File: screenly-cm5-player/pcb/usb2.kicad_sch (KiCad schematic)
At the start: 8 parts, among them J7 10.0 QHHTZB6.3, U7 AP22652W6-7

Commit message: Finished USB
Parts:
- removed R28: 100K, Screenly:R_0402, symbol Screenly:Resistor 100K 1% 0402 (0402WGF1003TCE)
- added R28: 31.6K, Screenly:R_0402, symbol Screenly:Resistor 31.6K 1% 0402 (0402WGF3162TCE)
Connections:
- net GND: now also J7.4 (GND), J7.SH, R28.2
- net at U7.5 (ILIM): now also R28.1
- net +5V renamed +5V_USB

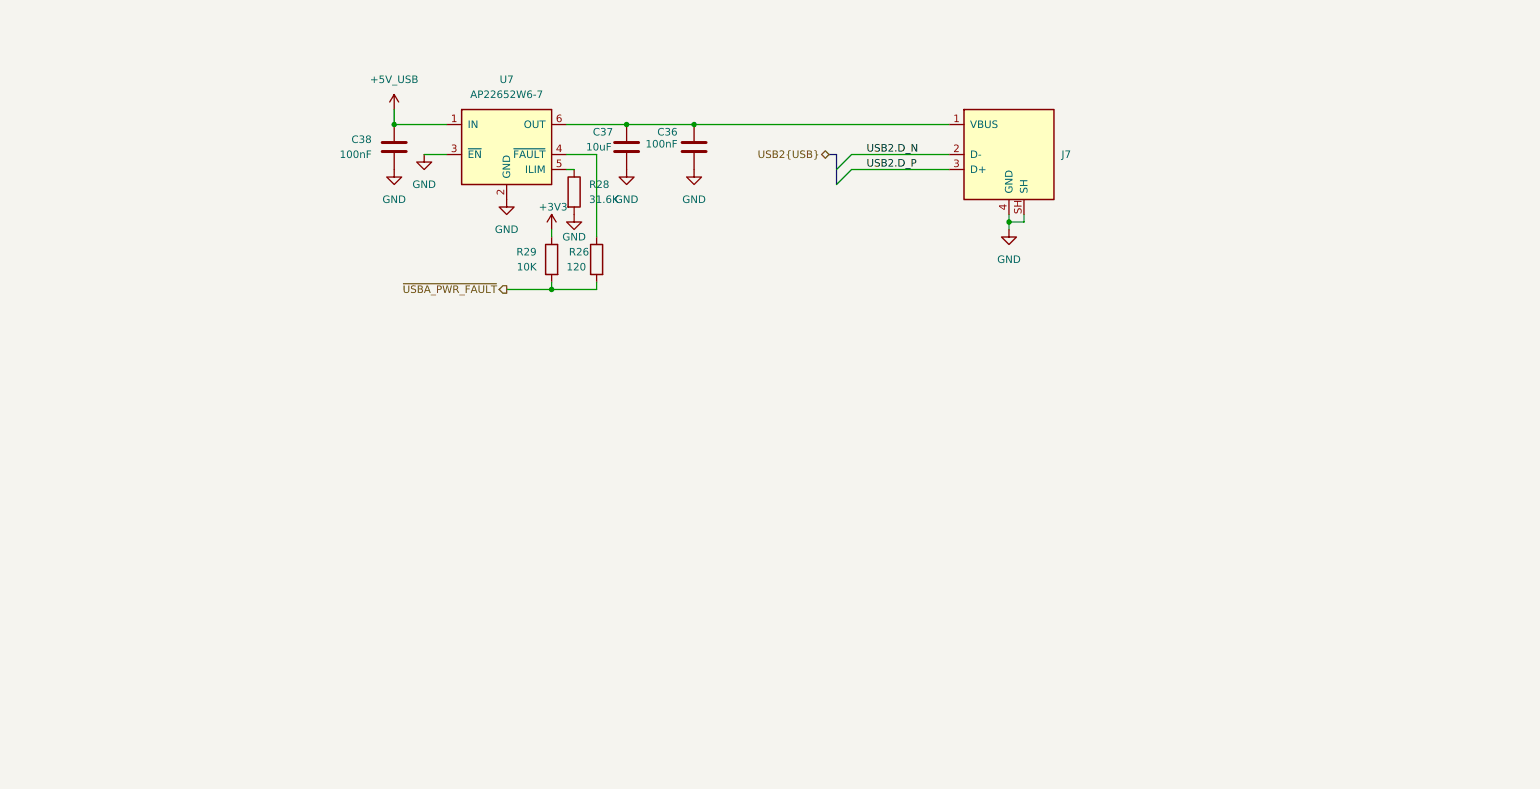
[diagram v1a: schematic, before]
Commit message: Revised USB design 1xUSB-C 2.0, 2xUSB-A 3.0
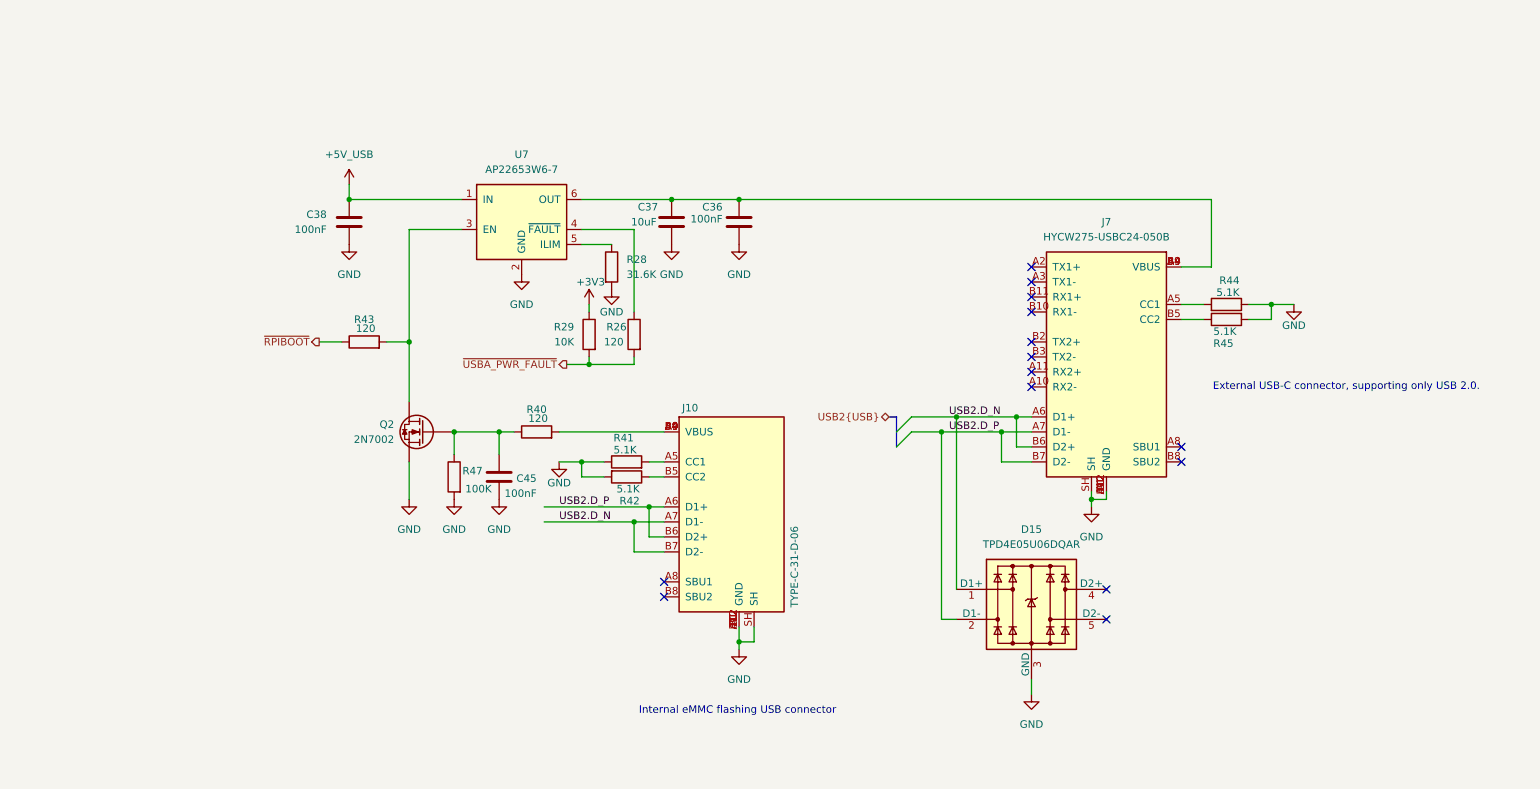
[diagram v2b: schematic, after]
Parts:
- removed J7: 10.0 QHHTZB6.3, Screenly:USB_A_SHOUHAN_QHHTZB6.3_Horizontal, symbol Screenly:USB-A Receptacle USB 2.0 SMD (10.0 QHHTZB6.3)
- removed U7: AP22652W6-7, Screenly:SOT-23-6, symbol Screenly:Power Switch 3-5.5V 2.1A SOT-23-6 (AP22652W6-7)
- added C45: 100nF, Screenly:C_0402, symbol Screenly:Capacitor 100nF 50V X7R 0402 (CL05B104KB54PNC)
- added D15: TPD4E05U06DQAR, Screenly:TI_USON-10_2.5x1.0mm_P0.5mm, symbol Screenly:ESD Diode 4ch 5.5V USON-10 (TPD4E05U06DQAR)
- added J10: TYPE-C-31-D-06, Screenly:USB_C_Receptacle_HRO_TYPE-C-31-D-06_Vertical, symbol Screenly:USB-C Receptacle 16P USB 2.0 Vertical SMD (TYPE-C-31-D-06)
- added J7: HYCW275-USBC24-050B, Screenly:USB_C_Receptacle_HOAUC_HYCW275-USBC24-050B, symbol Screenly:USB-C Receptacle 24P USB 3.1 SMD (HYCW275-USBC24-050B)
- added Q2: 2N7002, Screenly:SOT-23, symbol Screenly:N-MOSFET 60V 115mA 7.5Ohm SOT-23 (2N7002)
- added R40, R43: 120, Screenly:R_0402, symbol Screenly:Resistor 120R 5% 0402 (0402WGJ0121TCE)
- added R41, R42, R44, R45: 5.1K, Screenly:R_0402, symbol Screenly:Resistor 5.1K 1% 0402 (0402WGF5101TCE)
- added R47: 100K, Screenly:R_0402, symbol Screenly:Resistor 100K 1% 0402 (0402WGF1003TCE)
- added U7: AP22653W6-7, Screenly:SOT-23-6, symbol Screenly:Power Switch 3-5.5V 2.1A SOT-23-6 (AP22653W6-7)
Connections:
- net +5V_USB: now also U7.1 (IN)
- net GND: now also C45.2, D15.3 (GND), D15.8 (GND), J10.A1 (GND), J10.A12 (GND), J10.B1 (GND), J10.B12 (GND), J10.SH, J7.A1 (GND), J7.A12 (GND), J7.B1 (GND), J7.B12 (GND), J7.SH, Q2.2 (S), R41.1, R42.2, R44.1, R45.2, R47.2, U7.2 (GND)
- net USB2.D_N: now also D15.1 (D1+), D15.10, J10.A7 (D1-), J10.B7 (D2-), J7.A6 (D1+), J7.B6 (D2+)
- net USB2.D_P: now also D15.2 (D1-), D15.9, J10.A6 (D1+), J10.B6 (D2+), J7.A7 (D1-), J7.B7 (D2-)
- net at C36.1, C37.1: now also J7.A4 (VBUS), J7.A9 (VBUS), J7.B4 (VBUS), J7.B9 (VBUS), U7.6 (OUT)
- net at R26.1: now also U7.4 (~{FAULT})
- net at R28.1: now also U7.5 (ILIM)
- new net: J7.A5 (CC1), R44.2
- new net: J7.B5 (CC2), R45.1
- new net: J10.A4 (VBUS), J10.A9 (VBUS), J10.B4 (VBUS), J10.B9 (VBUS), R40.2
- new net: J10.A5 (CC1), R41.2
- new net: J10.B5 (CC2), R42.1
- new net: C45.1, Q2.1 (G), R40.1, R47.1
- new net: Q2.3 (D), R43.2, U7.3 (EN)
- new net: D15.4 (D2+), D15.7
- new net: D15.5 (D2-), D15.6
- new net ~{RPIBOOT}: R43.1
- no-connect marks 0 -> 14
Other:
- note added: "External USB-C connector, supporting only USB 2.0."
- note added: "Internal eMMC flashing USB connector"
- moved on the sheet: C36, C37, C38, R26, R28, R29

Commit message: Finished schematics design.
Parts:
- removed R44, R45: 5.1K, Screenly:R_0402, symbol Screenly:Resistor 5.1K 1% 0402 (0402WGF5101TCE)
- added R54, R55: 56K, Screenly:R_0402, symbol Screenly:Resistor 56K 1% 0402 (0402WGF5602TCE)
- added TP21, TP22, TP23, TP24, TP25: TestPoint, Screenly:TestPoint_Pad_D2.0mm, symbol Screenly:Test Point Pad 2.0mm
- renumbered C38 to C45, C45 to C46, C37 to C47, C36 to C48, D15 to D18, J7 to J11, R43 to R46, R40 to R48, R29 to R49, R28 to R50, R41 to R51, R42 to R52, R26 to R53, U7 to U9
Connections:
- net +5V_USB: now also R54.2, R55.2
- net GND: now also TP25.1
- net USB2.D_N: now also D18.2 (D1-), D18.9, J11.A7 (D1-), J11.B7 (D2-), TP24.1; no longer D18.1 (D1+), D18.10, J11.A6 (D1+), J11.B6 (D2+)
- net USB2.D_P: now also D18.1 (D1+), D18.10, J11.A6 (D1+), J11.B6 (D2+), TP23.1; no longer D18.2 (D1-), D18.9, J11.A7 (D1-), J11.B7 (D2-)
- net at C47.1, C48.1, J11.A4 (VBUS)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: now also TP22.1
- net at J11.A5 (CC1): now also R54.1
- net at J11.B5 (CC2): now also R55.1
- net at J10.A4 (VBUS), J10.A9 (VBUS), J10.B4 (VBUS)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: now also TP21.1
- net at D18.4 (D2+): no longer D18.7
- net at D18.5 (D2-): no longer D18.6
- net ~{USBA_PWR_FAULT} renamed ~{USB2_PWR_FAULT}
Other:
- note added: "USB connector for internal eMMC flashing"
- note removed: "Internal eMMC flashing USB connector"
- moved on the sheet: C45, C46, C47, C48, D18, Q2, R46, R47, R48, R49, R50, R51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

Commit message: Rough placements
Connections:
- net at D18.4 (D2+): now also D18.7
- net at D18.5 (D2-): now also D18.6
